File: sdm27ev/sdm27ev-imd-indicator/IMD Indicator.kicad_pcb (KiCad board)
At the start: 2 copper layers, 33 x 32.5 mm, 14 parts, among them J5 776280-1, Q1 2N7002,215, Q2 2N7002,215

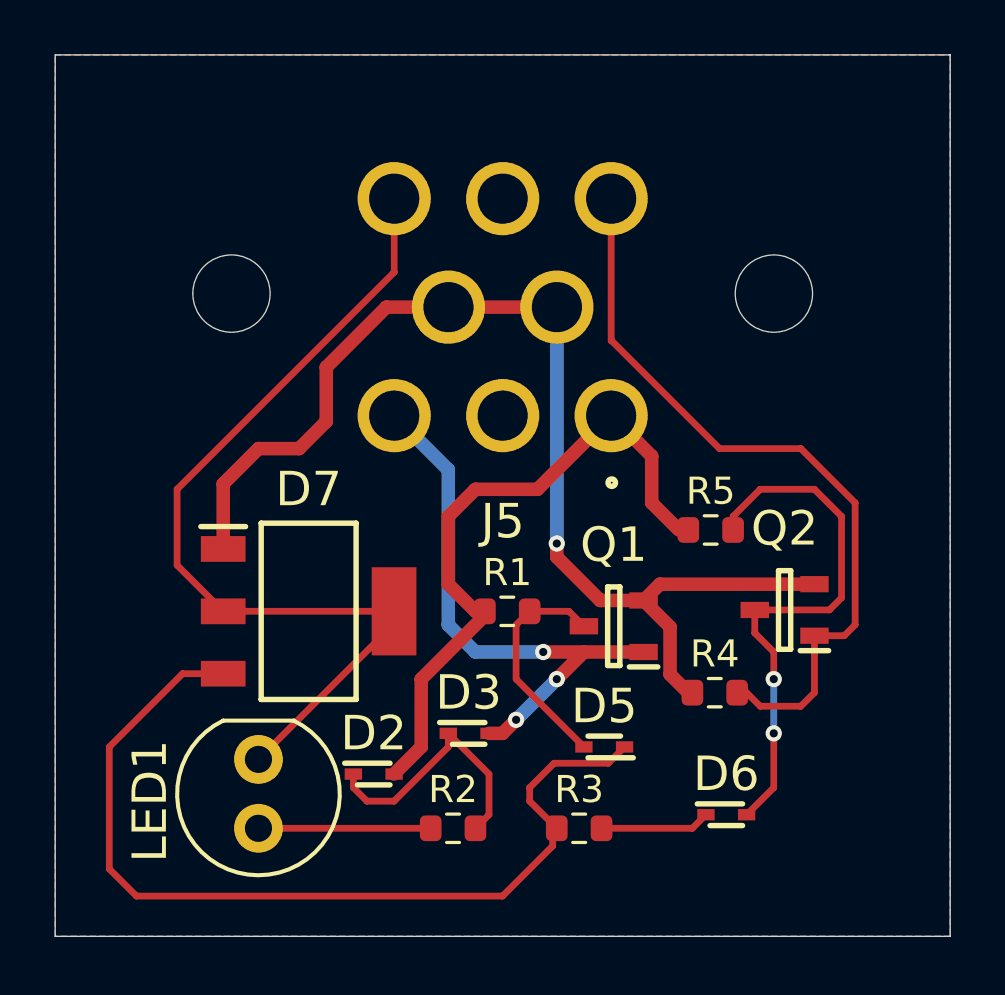
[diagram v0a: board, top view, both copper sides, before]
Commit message: IMD temp push for BOM
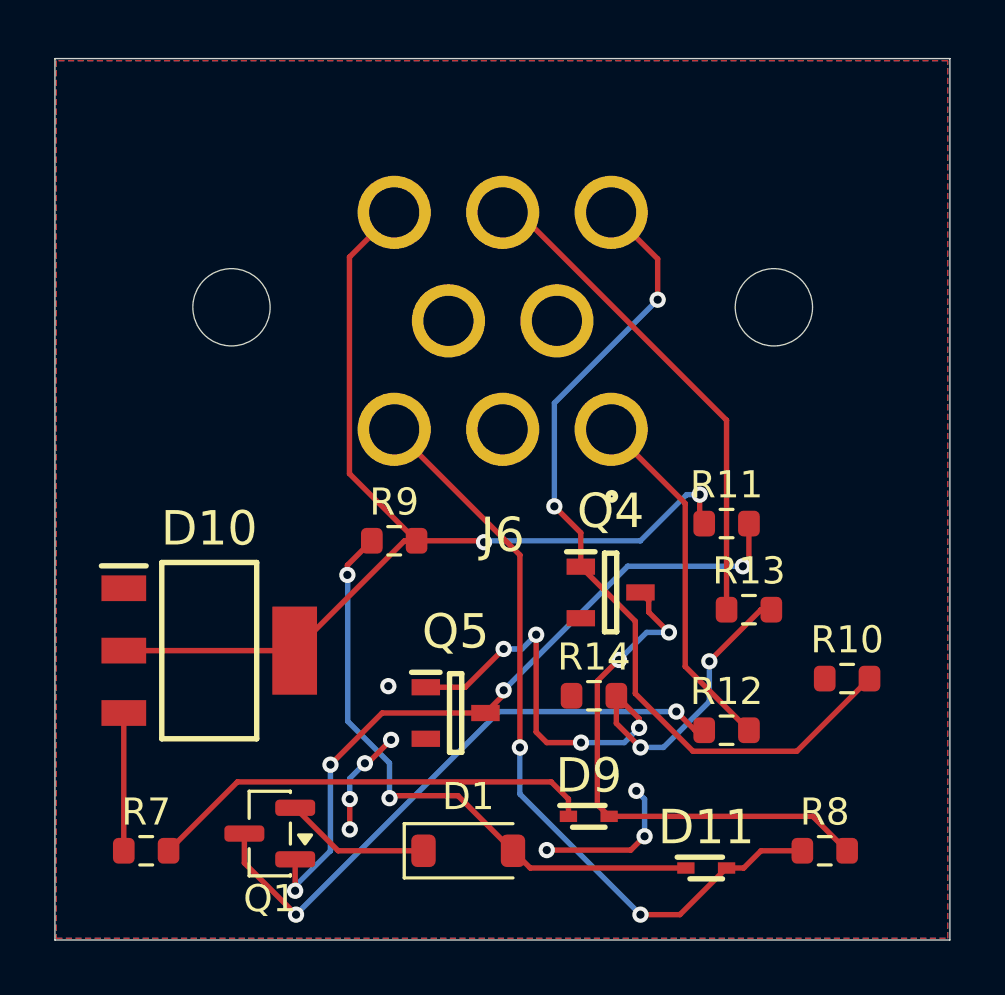
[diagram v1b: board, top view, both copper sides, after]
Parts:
- removed D2, D3, D5, D6: BAT54XV2T1G, SDM_MiscFootprint:SODFL1608X70N
- removed D7: X0202MN_5BA4, SDM_MiscFootprint:SOT230P700X190-4N
- removed J5: 776280-1, SDM_MiscFootprint:776280-1
- removed LED1: HLMP-EG30-NR000, IMDFootprintLibrary:LED_5MM
- removed Q2: 2N7002,215, SDM_MiscFootprint:SOT95P230X110-3N
- removed R1, R5: 10k, Resistor_SMD:R_0603_1608Metric
- removed R2: 510, Resistor_SMD:R_0603_1608Metric
- removed R3: 1k, Resistor_SMD:R_0603_1608Metric
- removed R4: 2.2k, Resistor_SMD:R_0603_1608Metric
- added D1: 1N4148, Diode_SMD:D_SOD-123, F.Cu at (164.7, 88.3)
- added D10: X0202MN_5BA4, SDM_MiscFootprint:SOT230P700X190-4N, F.Cu at (155.2, 80.9)
- added D11: BAT54XV2T1G, SDM_MiscFootprint:SODFL1608X70N, F.Cu at (173.5, 89.0)
- added D9: BAT54XV2T1G, SDM_MiscFootprint:SODFL1608X70N, F.Cu at (169.2, 87.1)
- added J6: 776280-1, IMDFootprintLibrary:776280-1, F.Cu at (166.0, 57.0)
- added Q4: 2N7002,215, SDM_MiscFootprint:SOT95P230X110-3N, F.Cu at (170.0, 78.8)
- added Q5: 2N7002,215, SDM_MiscFootprint:SOT95P230X110-3N, F.Cu at (164.3, 83.2)
- added R10: 2.2k, Resistor_SMD:R_0603_1608Metric, F.Cu at (178.7, 82.0)
- added R11: 47k, Resistor_SMD:R_0603_1608Metric, F.Cu at (174.3, 76.3)
- added R12: 560, Resistor_SMD:R_0603_1608Metric, F.Cu at (174.3, 83.9)
- added R13: 1k, Resistor_SMD:R_0603_1608Metric, F.Cu at (175.1, 79.4)
- added R14: 100k, Resistor_SMD:R_0603_1608Metric, F.Cu at (169.4, 82.6)
- added R7: 1k, Resistor_SMD:R_0603_1608Metric, F.Cu at (152.9, 88.3)
- added R8: 10k, Resistor_SMD:R_0603_1608Metric, F.Cu at (177.9, 88.3)
- added R9: 620, Resistor_SMD:R_0603_1608Metric, F.Cu at (162.0, 76.9)
- Q1: value 2N7002,215 -> BSS84; footprint SDM_MiscFootprint:SOT95P230X110-3N -> Package_TO_SOT_SMD:SOT-23
- moved Q1 14.8 mm to (157.4, 87.7)
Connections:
- Q1 pad 1: /12V MASTER -> Net-(Q1-G)
- Q1 pad 2: GND -> Net-(D1-K)
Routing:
- net GND: track 42.3 -> 9.61 mm, vias 1 -> 8
- net /SCR Gate: track 34.0 -> 5.08 mm
- net Net-(Q1-G): track 0.00 -> 26.4 mm, vias 0 -> 4
- net /12V IGNITION: track 24.4 -> 0.00 mm
- net Net-(Q5-G): track 0.00 -> 24.2 mm, vias 0 -> 6
- net Net-(D1-A): track 0.00 -> 22.6 mm, vias 0 -> 2
- net Net-(D6-A): track 20.0 -> 0.00 mm, vias 2 -> 0
- net Net-(D9-A): track 0.00 -> 19.8 mm, vias 0 -> 2
- net /LAMP_TEST: track 0.00 -> 18.4 mm
- net Net-(D9-K): track 0.00 -> 16.7 mm
- net Net-(Q1-D): track 8.47 -> 22.2 mm, vias 0 -> 2
- net /LED+: track 0.00 -> 13.2 mm
- net Net-(D2-K): track 9.86 -> 0.00 mm
- net /12V MASTER: track 20.9 -> 28.6 mm, vias 3 -> 2
- net Net-(LED1-A): track 6.35 -> 0.00 mm
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
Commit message: IMD complete
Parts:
- added TP1: GND_TEST, TestPoint:TestPoint_Pad_D1.5mm, F.Cu at (180.4, 63.8)
- added TP2: LED_TEST, TestPoint:TestPoint_Pad_D1.5mm, F.Cu at (179.7, 71.7)
- added TP3: KILL_TEST, TestPoint:TestPoint_Pad_D1.5mm, F.Cu at (178.5, 77.2)
- added TP4: SCR_TEST, TestPoint:TestPoint_Pad_D1.5mm, F.Cu at (151.7, 74.8)
- added TP5: Q4_TEST, TestPoint:TestPoint_Pad_D1.5mm, F.Cu at (180.3, 86.0)
- D1: value 1N4148 -> LED; footprint Diode_SMD:D_SOD-123 -> LED_SMD:LED_0805_2012Metric
- moved D1 1.32 mm to (164.0, 89.4)
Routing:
- net /LAMP_TEST: track 18.4 -> 29.4 mm, vias 0 -> 2
- net /SCR Gate: track 5.08 -> 14.6 mm
- net IMD KILL SIGNAL: track 38.6 -> 46.6 mm, vias 2 -> 3
- net Net-(Q1-G): track 26.4 -> 33.4 mm
- net Net-(D9-A): track 19.8 -> 22.7 mm
- net Net-(D1-A): track 22.6 -> 24.5 mm
- net Net-(Q1-D): track 22.2 -> 23.6 mm
- net /IMD_LOGIC_SIGNAL: track 31.9 -> 32.6 mm, vias 2 -> 1
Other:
- board text added: "GND"
- board text added: "KILL"
- board text added: "LED"
- board text added: "Q4"
- board text added: "SCR"
